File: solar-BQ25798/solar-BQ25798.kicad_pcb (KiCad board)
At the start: 4 copper layers, 177 x 85 mm, 356 parts, among them J101 Power In, J102 Power OUT, J103 Power OUT, J1901 TC2030, Q1001 DMP2035U-7, Q1002 Q_PMOS_GSD, Q1003 FS8205A_C908265, Q101 DMP4013LFGQ-13, Q102 2N7002, Q1101 DMP2035U-7, Q1102 Q_PMOS_GSD, Q1103 FS8205A_C908265, Q1201 DMP2035U-7, Q1202 Q_PMOS_GSD, Q1203 FS8205A_C908265, Q1301 DMP2035U-7, Q1302 Q_PMOS_GSD, Q1303 FS8205A_C908265, Q1401 DMP2035U-7, Q1402 Q_PMOS_GSD, Q1403 FS8205A_C908265, Q1501 DMP2035U-7, Q1502 Q_PMOS_GSD, Q1503 FS8205A_C908265, Q1601 DMP2035U-7, Q1602 Q_PMOS_GSD, Q1603 FS8205A_C908265, Q1801 CSD17578Q3A, Q1802 Q_PMOS_GSD, Q1803 CSD17578Q3A, Q1901 2N7002, Q201 DMP2035U-7, Q202 Q_PMOS_GSD, Q203 FS8205A_C908265, Q301 DMP2035U-7, Q302 Q_PMOS_GSD, Q303 FS8205A_C908265, Q401 DMP2035U-7, Q402 Q_PMOS_GSD, Q403 FS8205A_C908265, Q501 DMP2035U-7, Q502 Q_PMOS_GSD, Q503 FS8205A_C908265, Q601 DMP2035U-7, Q602 Q_PMOS_GSD, Q603 FS8205A_C908265, Q701 DMP2035U-7, Q702 Q_PMOS_GSD, Q703 FS8205A_C908265, Q801 DMP2035U-7, Q802 Q_PMOS_GSD, Q803 FS8205A_C908265, Q901 DMP2035U-7, Q902 Q_PMOS_GSD, Q903 FS8205A_C908265, U1001 BQ297xy, U101 HT75xx-1-SOT89, U102 INA219AxDCN, U106 M24C02-WMN, U1101 BQ297xy, U1201 BQ297xy, U1301 BQ297xy, U1401 BQ297xy, U1501 BQ297xy, U1601 BQ297xy, U1701 BQ25798RQMR, U1801 BQ76920PW, U1901 AHT20_C2757850, U1902 ATtiny1616-M, U201 BQ297xy, U301 BQ297xy, U401 BQ297xy, U501 BQ297xy, U601 BQ297xy, U701 BQ297xy, U801 BQ297xy, U901 BQ297xy

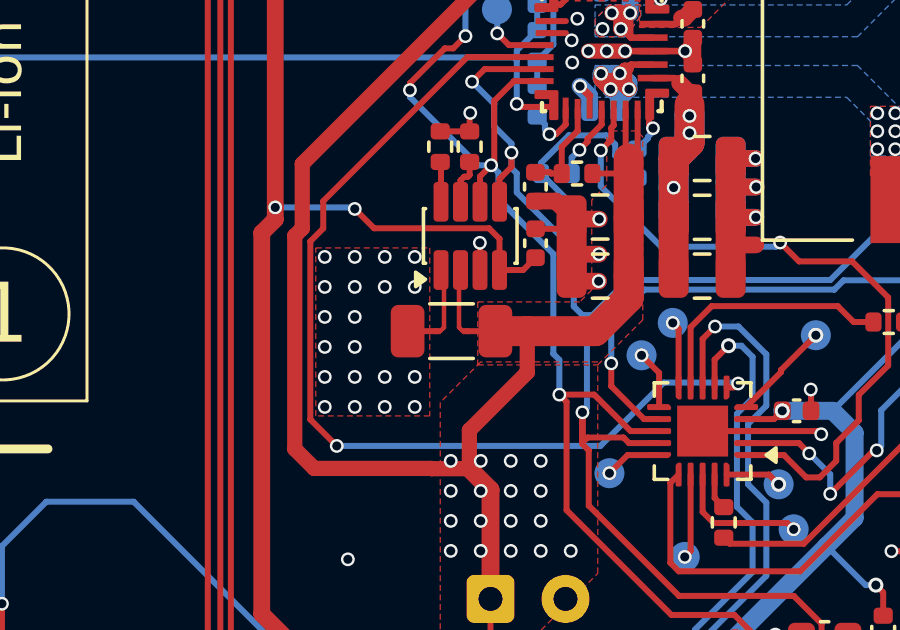
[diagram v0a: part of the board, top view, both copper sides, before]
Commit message: Improve optional shunt resistor
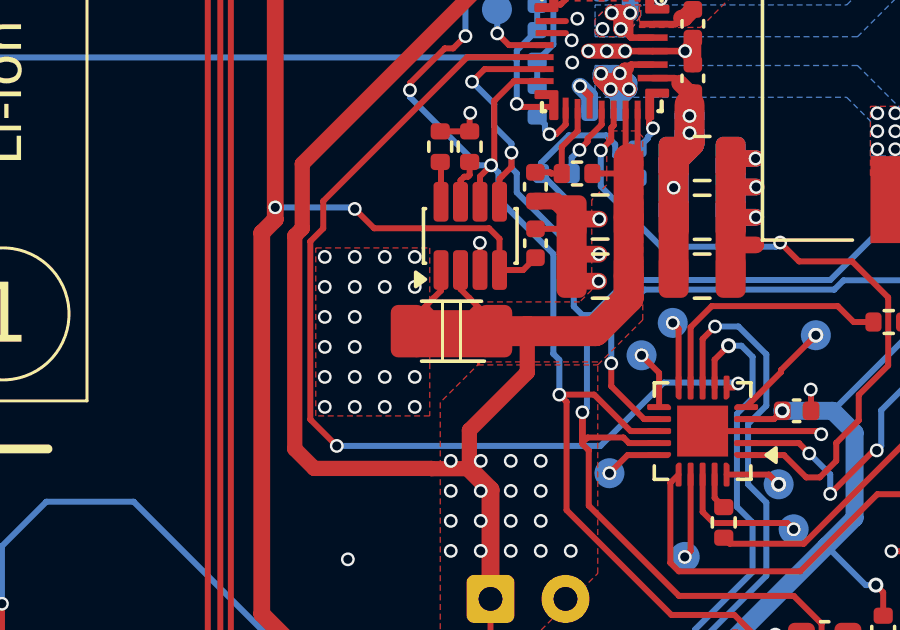
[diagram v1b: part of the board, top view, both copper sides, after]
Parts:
- J1901: footprint Connector:Tag-Connect_TC2030-IDC-NL_2x03_P1.27mm_Vertical -> cacophony-library:Tag-Connect_TC2030-IDC-NL_2x03_P1.27mm_Vertical
- R107: footprint cacophony-library:R_1206_Shunt -> cacophony-library:R_1206_Shunt_Short
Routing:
- net Net-(U102-IN+): track 2.13 -> 1.04 mm
- net Net-(U102-IN-): track 2.11 -> 1.06 mm

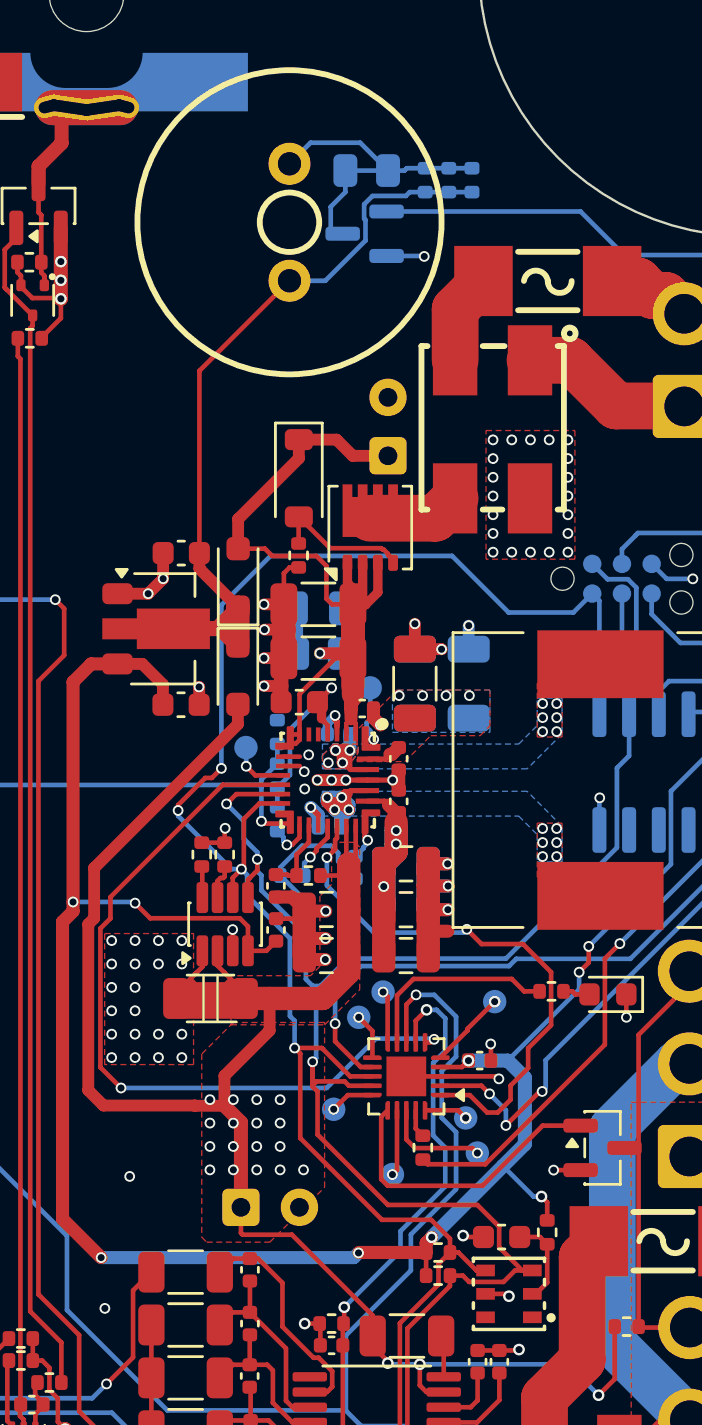
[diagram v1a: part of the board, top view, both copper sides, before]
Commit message: Reduce number of different resistor and capacitor values
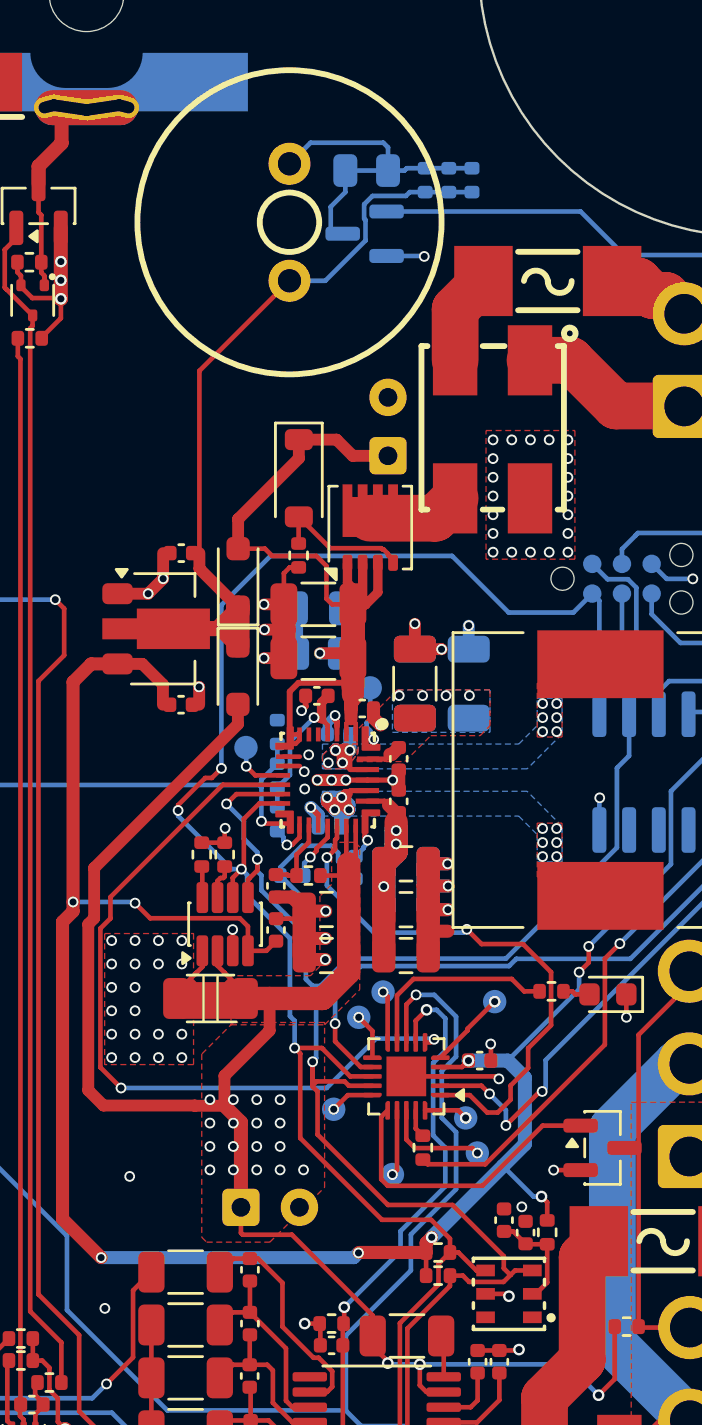
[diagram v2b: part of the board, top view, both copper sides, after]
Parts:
- removed C1901: 10uF, Capacitor_SMD:C_0603_1608Metric
- added C1814: 4.7uF, Capacitor_SMD:C_0402_1005Metric, F.Cu at (80.6, 12.6)
- added C1815: 4.7uF, Capacitor_SMD:C_0402_1005Metric, F.Cu at (81.5, 13.1)
- C101, C102, C1709: footprint Capacitor_SMD:C_0603_1608Metric -> Capacitor_SMD:C_0402_1005Metric
- C1705, C1708, C1717: value 100nF -> 100nF 50V
- C1812: value 4.7nF -> 1nF 50V
- R1814: value 470k -> 1M
- R1901: value 180Ω -> 330Ω
- moved C1709 0.80 mm to (72.6, -9.86)
- turned R1902 to 0 degrees
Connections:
- BUZZER1901 pad 2: Net-(BUZZER1901-Pad2) -> Net-(R1902-B)
- R1902 pad 1: Net-(BUZZER1901-Pad2) -> Net-(Q1901-D)
- R1902 pad 2: Net-(Q1901-D) -> Net-(R1902-B)
- R2 pad 2: Net-(BUZZER1901-Pad2) -> Net-(R1902-B)
- R3 pad 2: Net-(BUZZER1901-Pad2) -> Net-(R1902-B)
- R4 pad 2: Net-(BUZZER1901-Pad2) -> Net-(R1902-B)
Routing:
- net Net-(R1902-B): track 0.00 -> 9.29 mm
- net Net-(BUZZER1901-Pad2): track 8.71 -> 0.00 mm
- net GND: track 127.5 -> 124.7 mm
- net REGN: track 8.23 -> 6.69 mm
- net SCL: track 76.2 -> 75.1 mm
- net /ATtiny1616/AHT20_VDD: track 3.62 -> 4.39 mm
- net V_{IN}: track 41.2 -> 41.7 mm

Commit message: Update components LCSC parts
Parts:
- R1701: value 2Ω -> 2.2Ω
